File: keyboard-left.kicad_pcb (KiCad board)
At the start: 2 copper layers, 16.8 x 16.8 mm, 331 parts, among them J1 ST-Link Clone (Optional), K1 Esc,,,,,,,,,F1, K10 !,1,,,,,,,,A2, K11 @,2,,,,,,,,A3, K12 #,3,,,,,,,,A4, K13 $,4,,,,,,,,A5, K14 %,5,,,,,,,,A6, K15 ^,6,,,,,,,,A7, K16 Tab,,,,1.5,,,,,B1, K17 Q,,,,,,,,,B2, K18 W,,,,,,,,,B3, K19 E,,,,,,,,,B4, K2 F1,,,,,,,,,F2, K20 R,,,,,,,,,B5, K21 T,,,,,,,,,B6, K22 Caps Lock,,,,1.75,,,,,C1, K23 A,,,,,,,,,C2, K24 S,,,,,,,,,C3, K25 D,,,,,,,,,C4, K26 F,,,,,,,,,C5, K27 G,,,,,,,,,C6, K28 Shift,,,,2.25,,,,,D1, K29 Z,,,,,,,,,D2, K3 F2,,,,,,,,,F3, K30 X,,,,,,,,,D3, K31 C,,,,,,,,,D4, K32 V,,,,,,,,,D5, K33 B,,,,,,,,,D6, K34 Ctrl,,,,1.25,,,,,E1, K35 Win,,,,1.25,,,,,E2, K36 Alt,,,,1.25,,,,,E3, K37 Space,,,,3.00,,,,,E4, K4 F3,,,,,,,,,F4, K5 F4,,,,,,,,,F5, K6 F5,,,,,,,,,F6, K7 F6,,,,,,,,,F7, K9 ~,`,,,,,,,,A1, Q1 AO3401A, Q2 AO3401A, Q3 AO3401A, Q4 2N7002, Q5 2N7002, Q6 MMUN2133LT1G, Q7 AO3401A, Q8 MMUN2233LT1G, SW1 SW_Push, SW10 SW_Push, SW11 SW_Push, SW12 SW_Push, SW13 SW_Push, SW14 SW_Push, SW15 SW_Push, SW16 SW_Push, SW17 SW_Push, SW18 SW_Push, SW19 SW_Push, SW2 SW_Push, SW20 SW_Push, SW21 SW_Push, SW22 SW_Push, SW23 SW_Push, SW24 SW_Push, SW25 SW_Push, SW26 SW_Push, SW27 SW_Push, SW28 SW_Push, SW29 SW_Push, SW3 SW_Push, SW30 SW_Push, SW31 SW_Push, SW32 SW_Push, SW33 SW_Push, SW34 SW_Push, SW35 SW_Push, SW36 SW_Push, SW4 SW_Push, SW5 SW_Push, SW6 SW_Push, SW7 SW_Push, SW8 SW_Push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

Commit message: Started placing MCU support group
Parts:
- removed U2: STM32G474RETx, DjinnFootprints:STM32G474RETx
- moved F2 440.2 mm to (194.2, -7.62)
- moved U7 384.1 mm to (180.1, -9.21)
- moved C6 329.9 mm to (69.7, -47.4)
- moved U8 298.3 mm to (59.6, -46.7)
- moved F1 280.6 mm to (39.2, 27.9)
- moved U6 250.8 mm to (49.5, 18.7)
- moved U5 240.4 mm to (40.4, 18.7)
- moved C9 201.7 mm to (-24.0, 67.3), turned to 180 degrees
- moved C14 176.7 mm to (-35.5, 88.9), turned to 180 degrees
- moved U3 167.7 mm to (-15.5, 69.6), turned to -90 degrees
- moved U4 162.6 mm to (-24.1, 62.5)
- moved U11 155.1 mm to (-15.2, 124.5), turned to 90 degrees
- moved C7 145.2 mm to (-16.5, 64.8)
- moved C8 143.2 mm to (-16.5, 74.9)
- moved C26 139.4 mm to (-20.9, 78.7), turned to -90 degrees
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
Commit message: Start with USB support
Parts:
- moved FB12 357.0 mm to (-15.2, -218.5), turned to 90 degrees
- moved R2 342.5 mm to (-40.1, -202.0)
- moved R6 342.5 mm to (-34.3, -217.7)
- moved R9 342.5 mm to (-34.3, -208.3)
- moved F1 241.1 mm to (-14.3, -207.1)
- moved USB1 241.1 mm to (-12.7, -228.6)
- moved U5 232.0 mm to (-2.80, -209.2)
- moved U6 226.7 mm to (-11.4, -199.7), turned to 90 degrees
- moved Q2 225.7 mm to (4.96, -224.4)
- moved D40 225.7 mm to (-30.0, -233.7)
- moved Q1 225.7 mm to (4.96, -228.8)
- moved U11 15.7 mm to (-19.1, 109.2)
- moved RESET1 7.62 mm to (20.3, 5.08)

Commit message: Minor progress on component grouping
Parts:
- moved FB13 349.4 mm to (183.7, -17.1)
- moved R10 349.4 mm to (189.6, -13.9)
- moved R11 349.4 mm to (189.6, -10.8)
- moved R12 349.4 mm to (189.6, -7.62)
- moved R3 349.4 mm to (183.7, -7.62)
- moved R4 349.4 mm to (183.7, -4.47)
- moved R7 349.4 mm to (189.6, -23.4)
- moved D41 312.6 mm to (177.4, -30.6)
- moved Q3 312.6 mm to (202.5, -33.6)
- moved D39 272.6 mm to (-176.6, -116.2)
- moved D40 267.5 mm to (35.6, 25.7), turned to 180 degrees
- moved Q2 265.1 mm to (32.1, 39.3), turned to 90 degrees
- moved Q1 261.6 mm to (32.1, 31.4), turned to 90 degrees
- moved R6 259.4 mm to (37.1, 31.7)
- moved R9 252.8 mm to (37.1, 34.2)
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
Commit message: More component groupings
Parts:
- SPLIT1, USB1: footprint reversible-kicad-footprints:HRO-TYPE-C-31-M-12-HandSoldering-NoSBU -> Type-C.pretty-master:HRO-TYPE-C-31-M-12-HandSoldering
- moved C11 362.4 mm to (197.9, 150.8)
- moved C13 362.4 mm to (224.5, 143.2)
- moved Q5 362.4 mm to (196.7, 144.1)
- moved R13 362.4 mm to (220.8, 158.8)
- moved R14 362.4 mm to (208.1, 135.7)
- moved R17 362.4 mm to (208.1, 145.2)
- moved R18 362.4 mm to (208.1, 148.3)
- moved R19 362.4 mm to (208.1, 151.5)
- moved R22 362.4 mm to (208.1, 160.9)
- moved R24 362.4 mm to (214.0, 135.7)
- moved U8 362.4 mm to (226.1, 149.9)
- moved Q4 362.4 mm to (196.7, 139.7)
- moved R15 362.4 mm to (208.1, 138.9)
- moved R16 362.4 mm to (208.1, 142.0)
- moved R20 362.4 mm to (208.1, 154.6)
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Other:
- board size 16.8 x 16.8 mm -> 193 x 144.8 mm

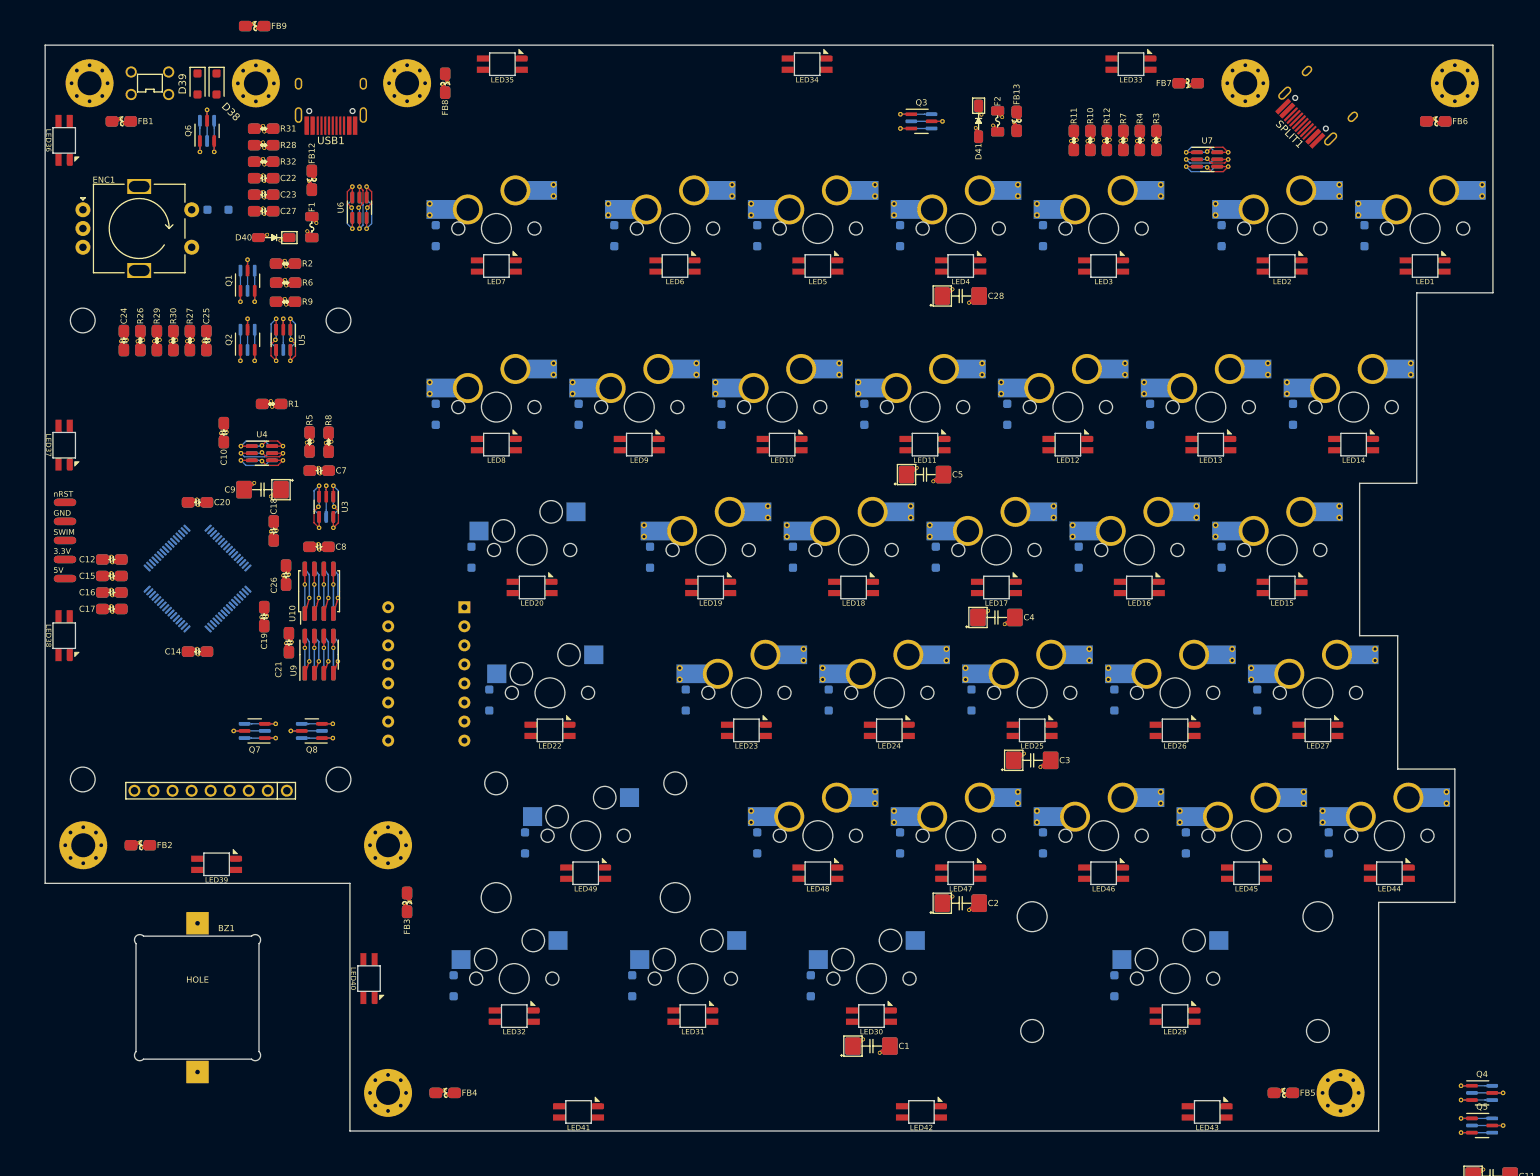
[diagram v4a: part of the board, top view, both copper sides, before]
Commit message: Board layout drawings added
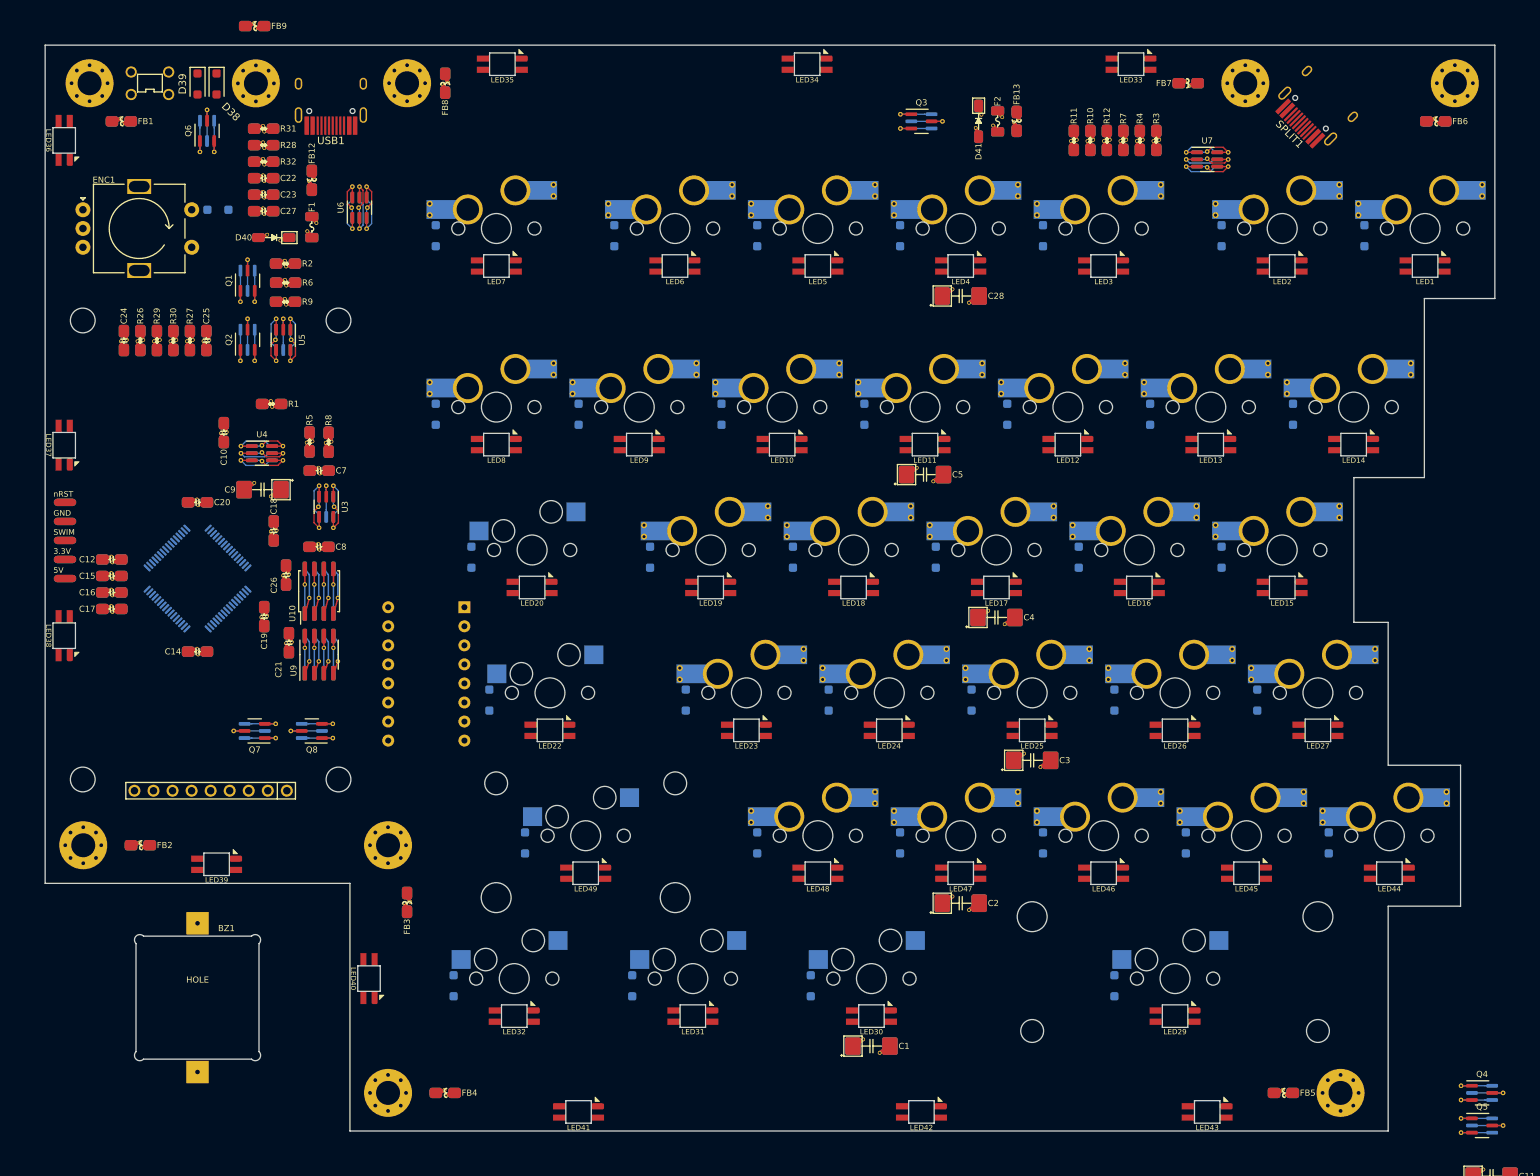
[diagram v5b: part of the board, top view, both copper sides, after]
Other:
- board size 193 x 144.8 mm -> 193.3 x 144.8 mm

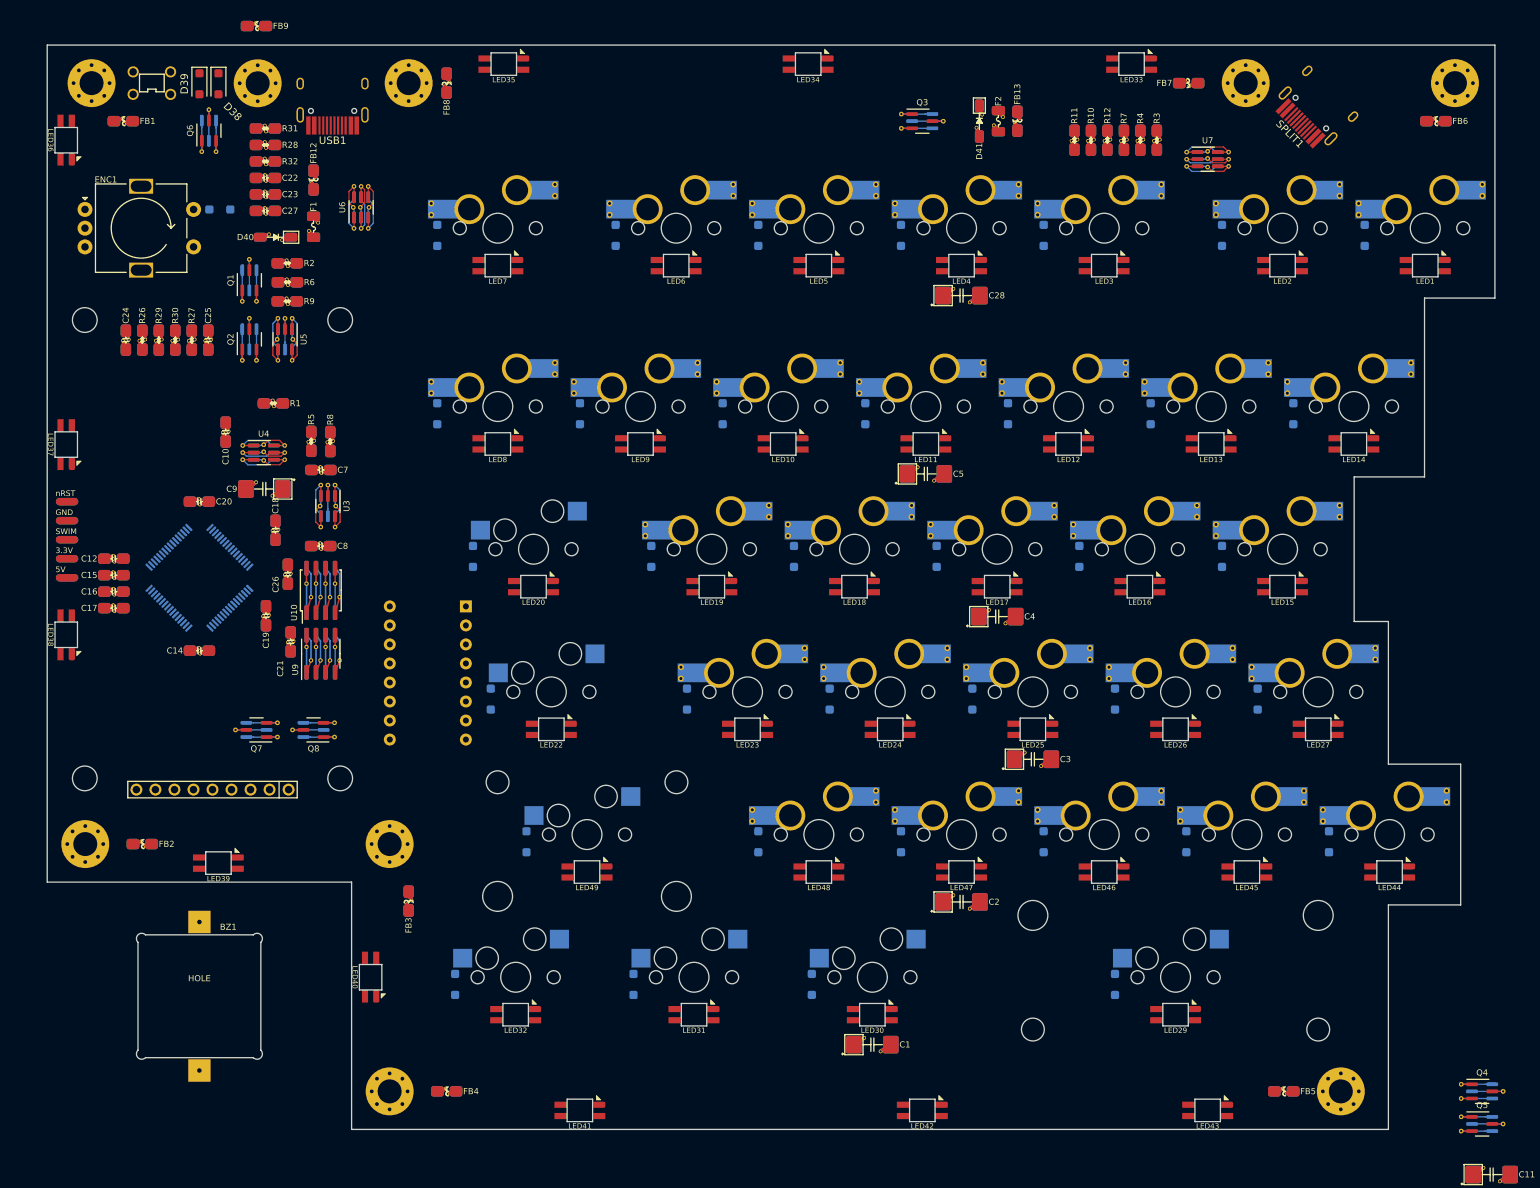
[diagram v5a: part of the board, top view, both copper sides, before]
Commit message: LED Flips
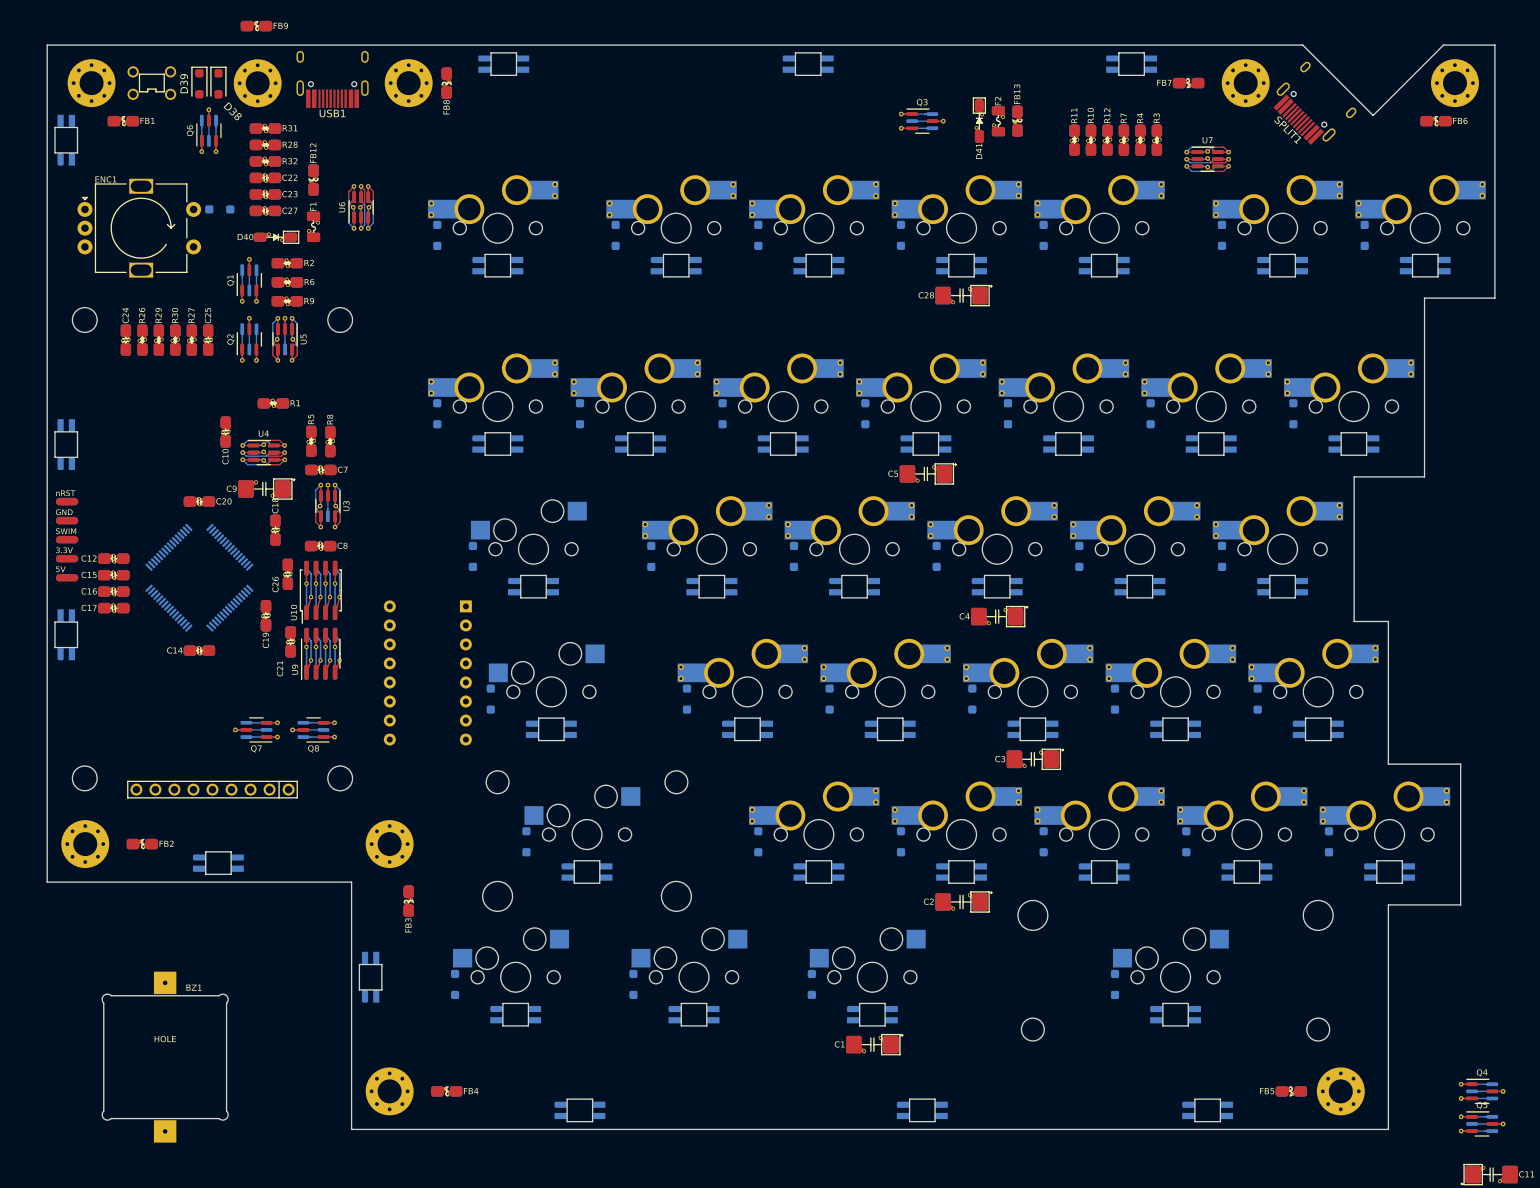
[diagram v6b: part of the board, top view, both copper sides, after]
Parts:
- C1, C2, C28, C3, C4, C5, LED1, LED10, LED11, LED12, LED13, LED14, LED15, LED16, LED17, LED18, LED19, LED2, LED20, LED22, LED23, LED24, LED25, LED26, LED27, LED29, LED3, LED30, LED31, LED32, LED33, LED34, LED35, LED36, LED37, LED38, LED39, LED4, LED40, LED41, LED42, LED43, LED44, LED45, LED46, LED47, LED48, LED49, LED5, LED6, LED7, LED8, LED9: moved to B.Cu
- moved BZ1 9.33 mm to (20.8, 135.1)
- moved USB1 3.57 mm to (43.2, -1.03)
- moved FB5 1.02 mm to (171.2, 139.7), turned to 180 degrees
- moved SPLIT1 0.57 mm to (178.0, 4.15)
- turned C1 to 180 degrees
- turned C2 to 180 degrees
- turned C28 to 180 degrees
- turned C3 to 180 degrees
- turned C4 to 180 degrees
- turned C5 to 180 degrees
- turned LED1 to 180 degrees
- turned LED10 to 180 degrees
- turned LED11 to 180 degrees
- turned LED12 to 180 degrees
- turned LED13 to 180 degrees
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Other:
- outline, holes or cut-outs redrawn
